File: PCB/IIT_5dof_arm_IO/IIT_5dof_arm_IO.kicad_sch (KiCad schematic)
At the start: 100 parts, among them J1 Conn_01x05, J2 Conn_01x03, J3 Conn_02x03_Counter_Clockwise, J4 Conn_01x03, J5 Conn_01x04, J6 DE9_Plug_MountingHoles, Q1 2N7002, Q2 2N7002, Q3 2N7002, Q4 2N7002, SW1 SW_Push, SW10 SW_Push, SW11 SW_Push, SW12 SW_Push, SW13 SW_Push, SW14 SW_Push, SW15 SW_SPDT, SW2 SW_Push, SW3 SW_Push, SW4 SW_Push, SW5 SW_Push, SW6 SW_Push, SW7 RotaryEncoder_Switch, SW8 SW_Push, SW9 SW_Push, U1 ATmega328P-A, U2 MAX3232, Y1 16MHz

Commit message: PCB layout
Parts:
- removed R30, R36: 10k, Resistor_SMD:R_0805_2012Metric_Pad1.20x1.40mm_HandSolder, symbol Device:R
- added C15, C16, C17, C18, C19, C20, C21, C22, C23, C24, C25, C26: 10nF, Capacitor_SMD:C_0805_2012Metric_Pad1.18x1.45mm_HandSolder, symbol Device:C
- added R21, R22: 4.7k, Resistor_SMD:R_0805_2012Metric_Pad1.20x1.40mm_HandSolder, symbol Device:R
- D1, D10, D11, D12, D2, D3, D4, D5, D6, D7, D8, D9: footprint LED_THT:LED_D5.0mm -> Connector_Molex:Molex_KK-254_AE-6410-02A_1x02_P2.54mm_Vertical
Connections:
- net UIPanel_+5V: now also J3.5 (Pin_5), R21.1, R22.1; no longer J3.6 (Pin_6)
- net UIPanel_BUTT1A: now also U1.9 (PD5), C15.1; no longer U1.12 (PB0)
- net UIPanel_BUTT1B: now also U1.26 (PC3), C24.1; no longer U1.23 (PC0)
- net UIPanel_BUTT2A: now also U1.10 (PD6), C16.1; no longer U1.13 (PB1)
- net UIPanel_BUTT2B: now also U1.25 (PC2), C23.1; no longer U1.24 (PC1)
- net UIPanel_BUTT3A: now also U1.11 (PD7), C17.1; no longer U1.14 (PB2)
- net UIPanel_BUTT3B: now also U1.24 (PC1), C22.1; no longer U1.25 (PC2)
- net UIPanel_BUTT4A: now also U1.12 (PB0), C18.1; no longer U1.9 (PD5)
- net UIPanel_BUTT4B: now also U1.23 (PC0), C21.1; no longer U1.26 (PC3)
- net UIPanel_Buzz: now also U1.14 (PB2); no longer U1.11 (PD7)
- net UIPanel_Enc_BUTT: now also U1.2 (PD4); no longer U1.10 (PD6)
- net UIPanel_GND: now also J3.6 (Pin_6), C15.2, C16.2, C17.2, C18.2, C19.2, C20.2, C21.2, C22.2, C23.2, C24.2, C25.2, C26.2; no longer J3.4 (Pin_4)
- net UIPanel_SCL: now also R22.2
- net UIPanel_SDA: now also R21.2
- net UIPanel_BUTT5A: now reaches R28.2, R7.2
- net UIPanel_BUTT5A: now also SW5.2, U1.13 (PB1), C19.1; no longer Q3.3 (D)
- removed net UIPanel_BUTT5A__UIPanel_Prog_MISO: J3.1 (Pin_1), Q3.2 (S), SW5.2, U1.16 (PB4)
- net UIPanel_BUTT5B: no longer names the net of R13.2, R34.2
- net UIPanel_BUTT5B: now also Q3.3 (D); no longer SW13.1, U1.2 (PD4)
- net UIPanel_BUTT6A__UIPanel_Prog_SCK renamed UIPanel_BUTT6A__UIPanel_Prog_MOSI
- net UIPanel_BUTT6A__UIPanel_Prog_MOSI: now also J3.1 (Pin_1), U1.15 (PB3), C25.1; no longer J3.2 (Pin_2), U1.17 (PB5)
- net UIPanel_BUTT6B__UIPanel_Prog_MOSI renamed UIPanel_BUTT6B__UIPanel_Prog_MISO
- net UIPanel_BUTT6B__UIPanel_Prog_MISO: now also J3.2 (Pin_2), U1.16 (PB4), C26.1; no longer J3.5 (Pin_5), U1.15 (PB3)
- new net UIPanel_BUTT5B__UIPanel_Prog_SCK: C20.1, J3.4 (Pin_4), Q3.2 (S), SW13.1, U1.17 (PB5)
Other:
- moved on the sheet: D11, D5, Q3, R13, R23, R28, R34, R7, SW13, SW15, SW5

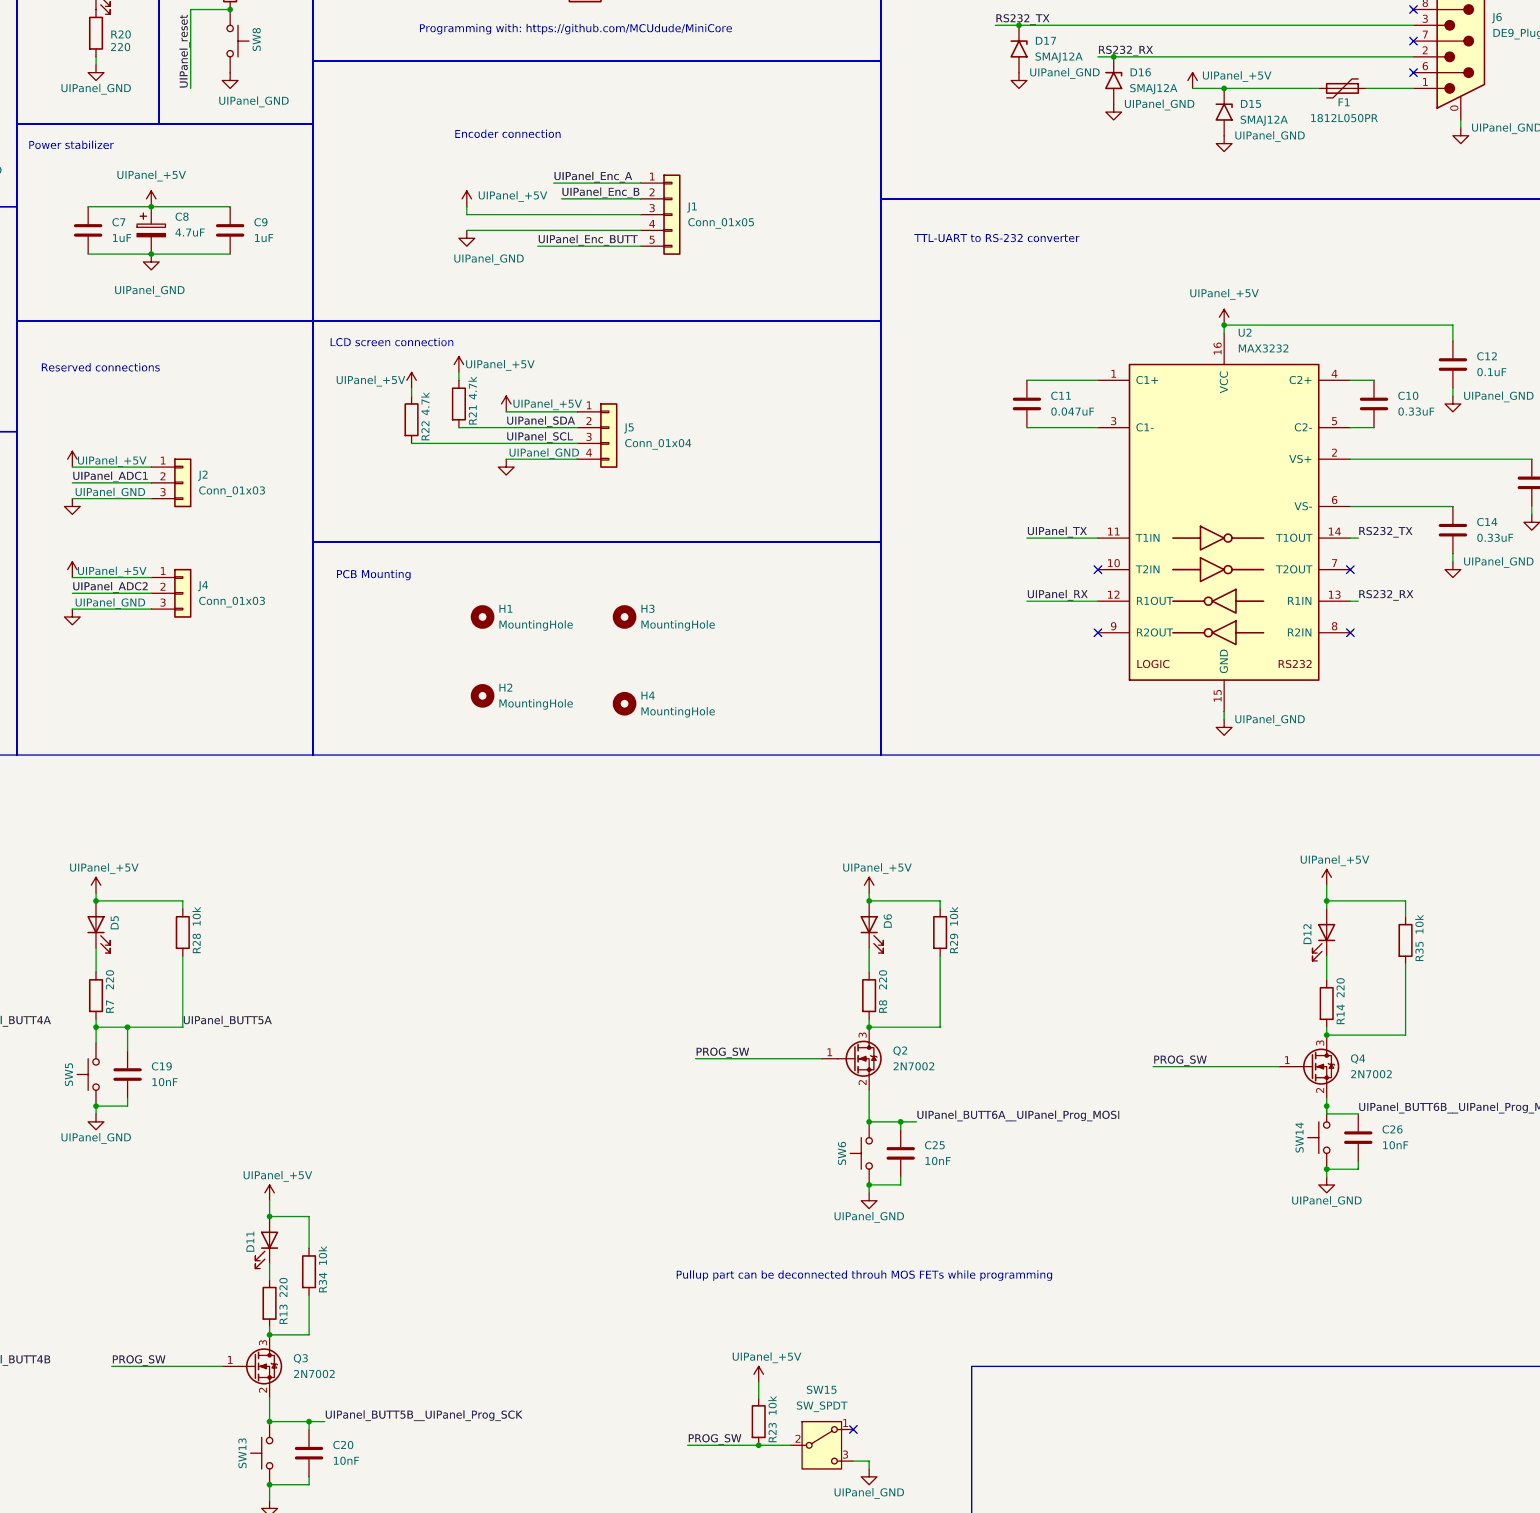
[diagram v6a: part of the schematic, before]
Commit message: Fix SMAJ value, program pullup switch
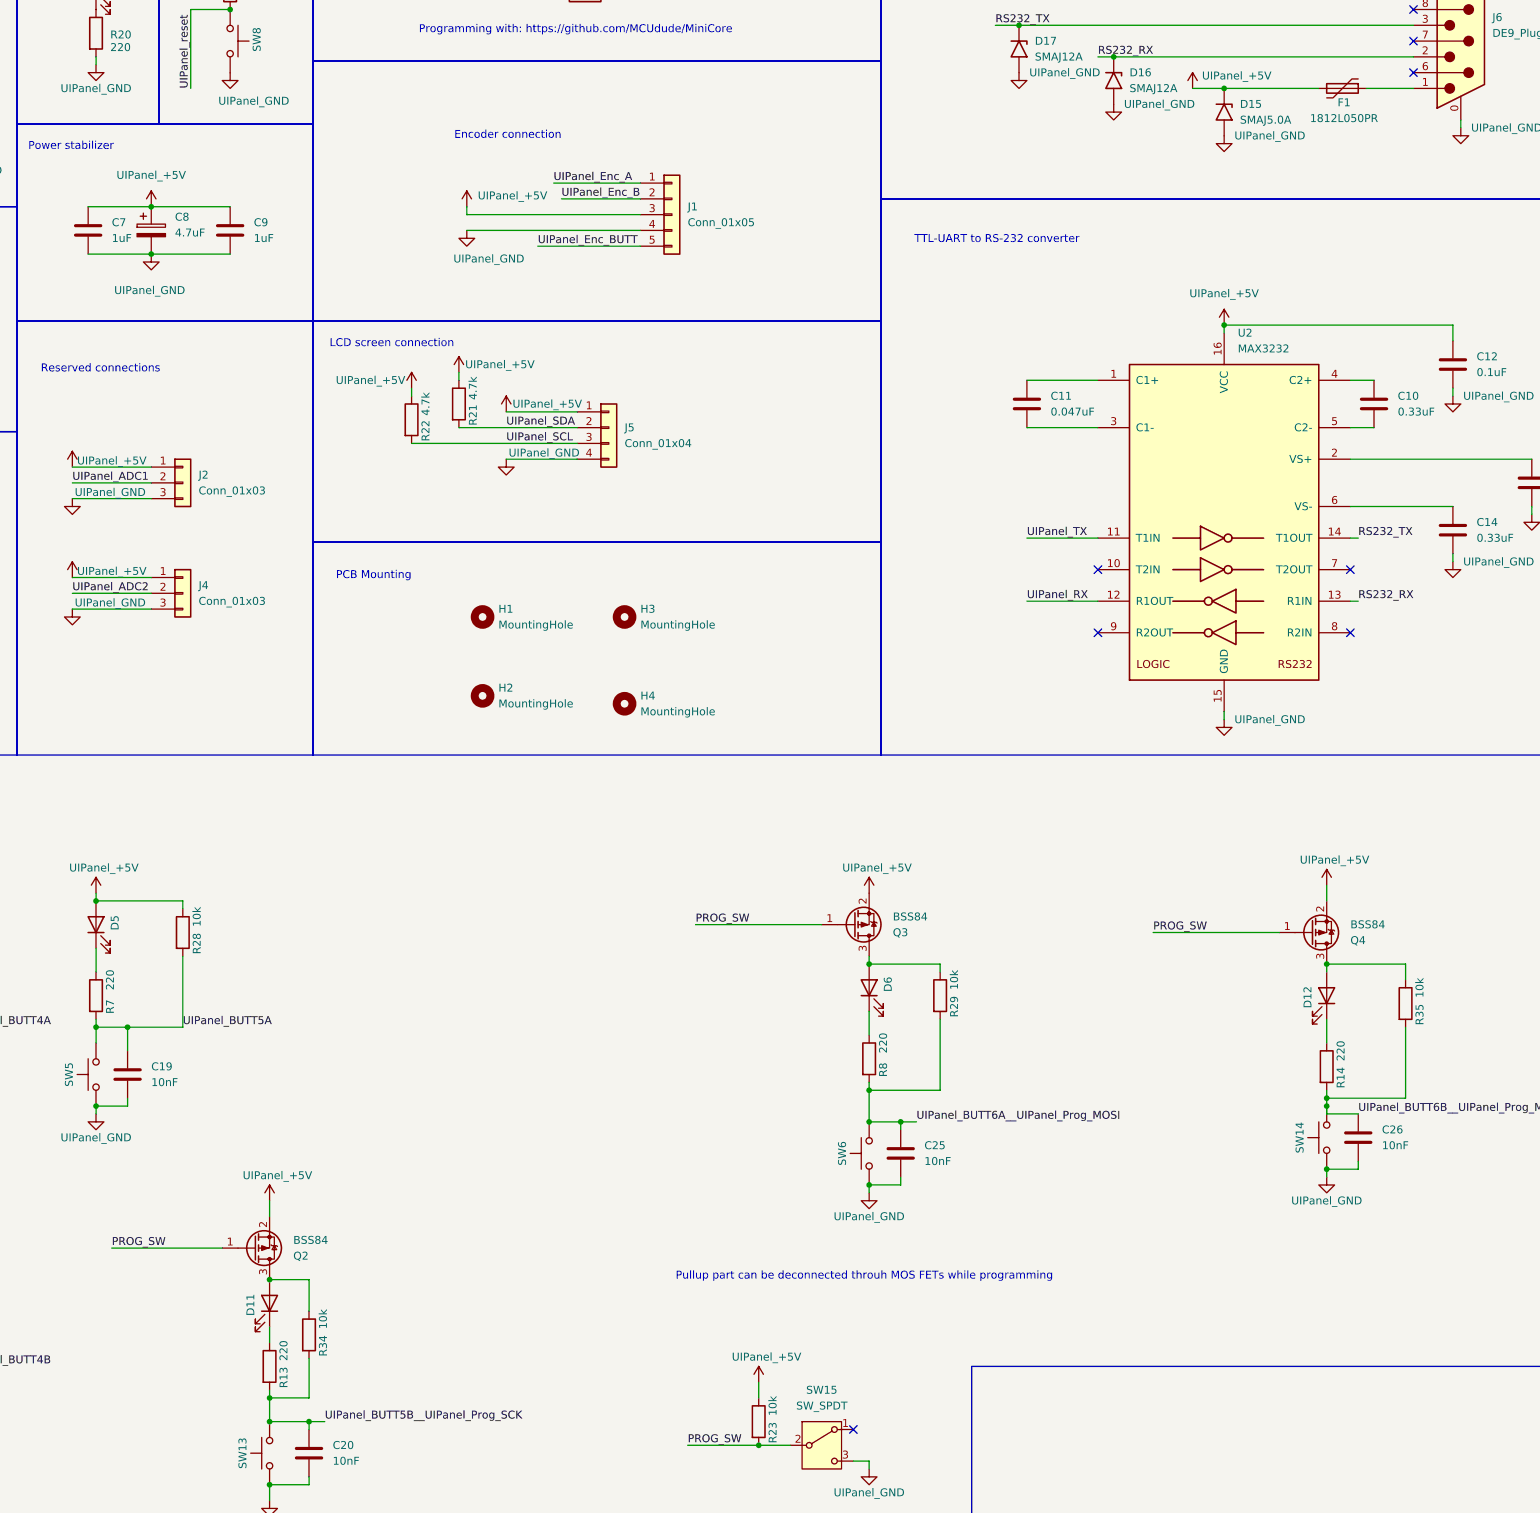
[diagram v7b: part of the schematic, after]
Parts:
- removed Q2, Q3, Q4: 2N7002, Package_TO_SOT_SMD:SOT-23, symbol Transistor_FET:2N7002
- added Q2, Q3, Q4: BSS84, Package_TO_SOT_SMD:SOT-23, symbol Transistor_FET:BSS84
- D15: value SMAJ12A -> SMAJ5.0A
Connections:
- net PROG_SW: now also Q2.1 (G), Q3.1 (G), Q4.1 (G)
- net UIPanel_+5V: now also Q2.2 (S), Q3.2 (S), Q4.2 (S); no longer D11.2 (A), D12.2 (A), D6.2 (A), R29.1, R34.1, R35.1
- net UIPanel_BUTT5B__UIPanel_Prog_SCK: now also R13.2, R34.2
- net UIPanel_BUTT6A__UIPanel_Prog_MOSI: now also R29.2, R8.2
- net UIPanel_BUTT6B__UIPanel_Prog_MISO: now also R14.2, R35.2
- new net: D6.2 (A), Q3.3 (D), R29.1
- new net: D12.2 (A), Q4.3 (D), R35.1
- new net: D11.2 (A), Q2.3 (D), R34.1
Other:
- moved on the sheet: D11, D12, D6, R13, R14, R29, R34, R35, R8

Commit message: Add potmeter, mot toggle to IO
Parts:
- removed J3: Conn_02x03_Counter_Clockwise, Connector_PinHeader_2.54mm:PinHeader_2x03_P2.54mm_Vertical, symbol Connector_Generic:Conn_02x03_Counter_Clockwise
- removed J4: Conn_01x03, Connector_Molex:Molex_KK-254_AE-6410-03A_1x03_P2.54mm_Vertical, symbol Connector_Generic:Conn_01x03
- added C27: 10nF, Capacitor_SMD:C_0805_2012Metric_Pad1.18x1.45mm_HandSolder, symbol Device:C
- added J10, J11, J12, J13, J14, J15, J16, J17, J18, J19, J20, J21, J22, J23, J24, J25, J26, J27, J28, J9: Conn_01x02, Connector_Molex:Molex_KK-254_AE-6410-04A_1x04_P2.54mm_Vertical, symbol Connector_Generic:Conn_01x02
- added J3: Conn_02x03_Odd_Even, symbol Connector_Generic:Conn_02x03_Odd_Even
- added J4, J7: Conn_01x02, symbol Connector_Generic:Conn_01x02
- added J8: Conn_01x04, Connector_Molex:Molex_KK-254_AE-6410-04A_1x04_P2.54mm_Vertical, symbol Connector_Generic:Conn_01x04
- added R30: 10k, Resistor_SMD:R_0805_2012Metric_Pad1.20x1.40mm_HandSolder, symbol Device:R
- added RV1: R_Potentiometer, symbol Device:R_Potentiometer
- added SW16: SW_Push, symbol Switch:SW_Push
- D1, D10, D11, D12, D14, D2, D3, D4, D5, D6, D7, D8, D9: footprint Connector_Molex:Molex_KK-254_AE-6410-02A_1x02_P2.54mm_Vertical -> LED_THT:LED_D5.0mm-3
- SW1, SW10, SW11, SW12, SW13, SW14, SW2, SW3, SW4, SW5, SW6, SW9: footprint Connector_Molex:Molex_KK-254_AE-6410-02A_1x02_P2.54mm_Vertical -> Button_Switch_THT:SW_PUSH-12mm
- SW7: footprint IIT_5dof_arm:Molex_for_encoder_1x05_P2.54mm_Vertical -> Rotary_Encoder:RotaryEncoder_Alps_EC12E-Switch_Vertical_H20mm
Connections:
- net UIPanel_+5V: now also J22.1 (Pin_1), J3.2 (Pin_2), J8.1 (Pin_1), R30.1, RV1.1
- net UIPanel_ADC1: now also RV1.2
- net UIPanel_ADC2: now also J4.1 (Pin_1); no longer U1.22 (ADC7)
- net UIPanel_BUTT5B__UIPanel_Prog_SCK: now also J3.3 (Pin_3)
- net UIPanel_BUTT6A__UIPanel_Prog_MOSI: now also J3.4 (Pin_4)
- net UIPanel_BUTT6B__UIPanel_Prog_MISO: now also J3.1 (Pin_1)
- net UIPanel_GND: now also C27.2, J3.6 (Pin_6), J4.2 (Pin_2), J7.2 (Pin_2), J8.4 (Pin_4), RV1.3, SW16.1
- net UIPanel_RX: now also J8.2 (Pin_2)
- net UIPanel_TX: now also J8.3 (Pin_3)
- net UIPanel_reset: now also J3.5 (Pin_5), J7.1 (Pin_1)
- net 5V_LED-: now reaches D14.1 (K), R20.1
- net 5V_LED-: now also J22.2 (Pin_2)
- new net ToggleMotors: C27.1, R30.2, SW16.2, U1.22 (ADC7)
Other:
- note added: "UART TTL connection"
- note removed: "Encoder connection"
- note removed: "Reserved connections"
- moved on the sheet: D14, J1
